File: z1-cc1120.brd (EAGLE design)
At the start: 100 x 50 mm, 11 parts, among them X1 PN61729-S

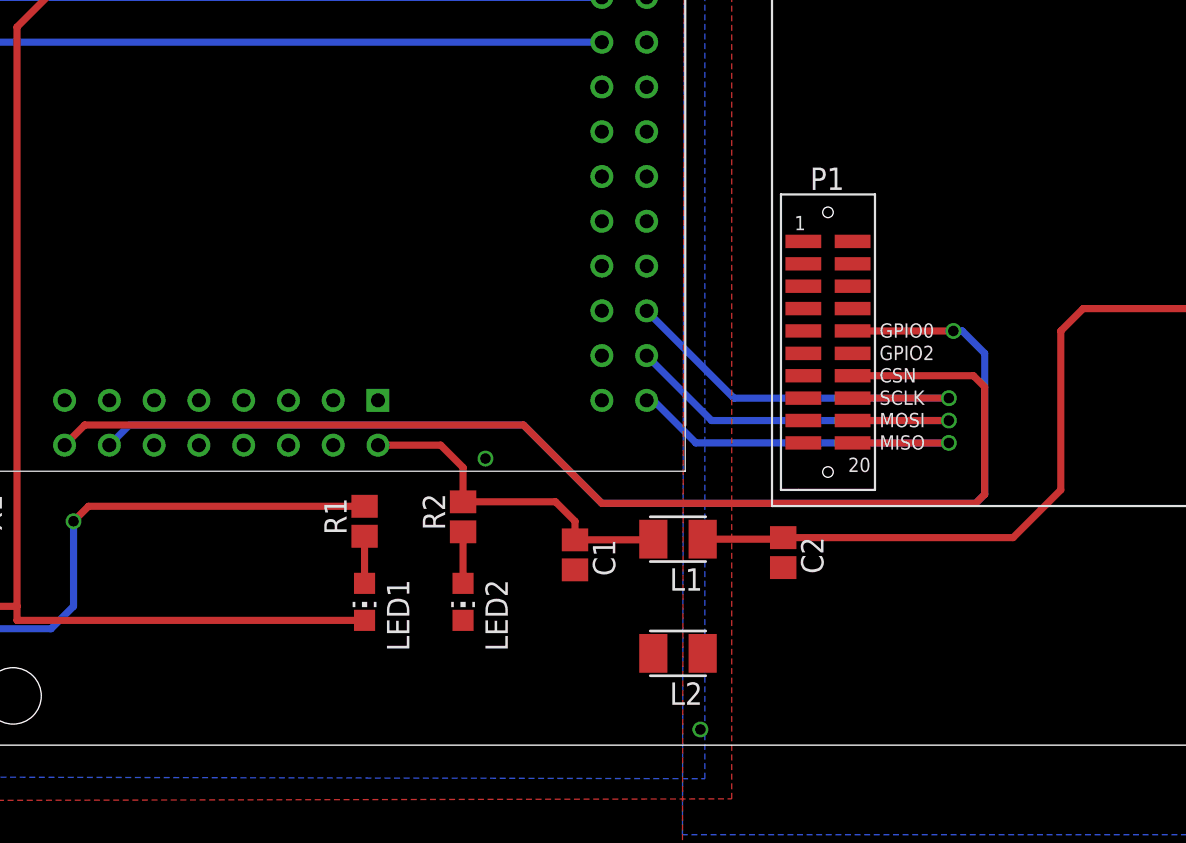
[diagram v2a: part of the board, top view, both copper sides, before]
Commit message: added header to ease radio debug
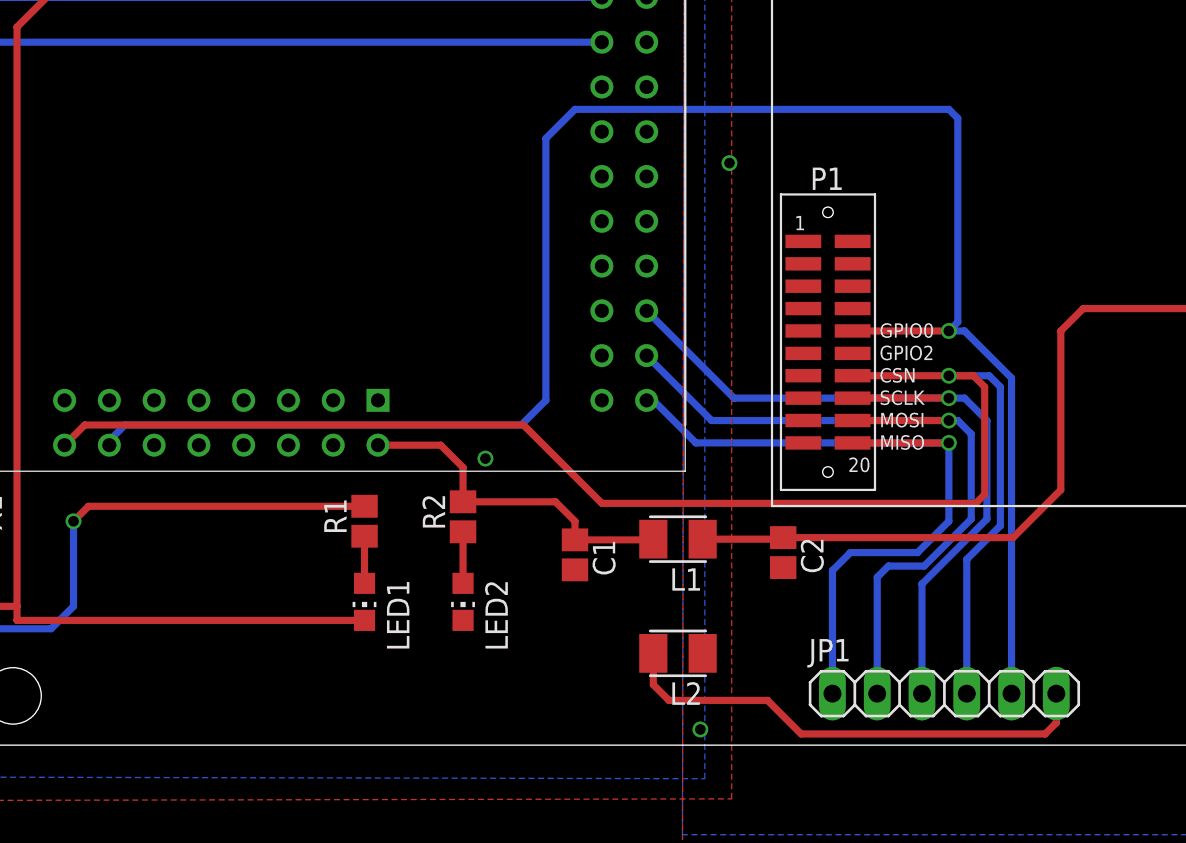
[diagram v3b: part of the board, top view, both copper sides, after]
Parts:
- added JP1: (no value), pinhead:1X06
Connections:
- net GND: now also JP1.6
- net RADIO_CSN: now also JP1.4
- net RADIO_INT: now also JP1.5
- net SPI_CLK: now also JP1.3
- net SPI_SIMO: now also JP1.2
- net SPI_SOMI: now also JP1.1
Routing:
- net RADIO_INT: track 68.2 -> 105.4 mm
- net GND: track 0.00 -> 27.7 mm
- net RADIO_CSN: track 68.6 -> 89.9 mm, vias 0 -> 1
- net SPI_SIMO: track 24.1 -> 43.8 mm
- net SPI_CLK: track 24.7 -> 44.4 mm
- net SPI_SOMI: track 23.6 -> 42.8 mm
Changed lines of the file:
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@@
 <text x="72.898" y="7.747" size="1.778" layer="51">Version 0.1</text>
 <text x="72.898" y="5.715" size="1.778" layer="51">Mountain Sensing</text>
-<text x="72.898" y="3.683" size="1.778" layer="51">PJB</text>
+<text x="22.987" y="1.27" size="1.778" layer="51">PJB</text>
 </plain>
 <attributes>
@@
 <element name="L1" library="resistor" package="L3230M" value="10mH" x="56.388" y="11.684" rot="R180"/>
 <element name="L2" library="resistor" package="L3230M" value="10mH" x="56.388" y="5.207" rot="R180"/>
+<element name="JP1" library="pinhead" package="1X06" value="" x="71.501" y="2.921"/>
 </elements>
 <signals>
@@
 <contactref element="L2" pad="2"/>
 <via x="45.466" y="16.256" extent="1-16" drill="0.6" shape="octagon"/>
+<contactref element="JP1" pad="6"/>
+<wire x1="54.988" y1="5.207" x2="54.988" y2="3.432" width="0.4064" layer="1"/>
+<wire x1="54.988" y1="3.432" x2="55.88" y2="2.54" width="0.4064" layer="1"/>
+<wire x1="55.88" y1="2.54" x2="61.468" y2="2.54" width="0.4064" layer="1"/>
+<wire x1="61.468" y1="2.54" x2="63.373" y2="0.635" width="0.4064" layer="1"/>
+<wire x1="63.373" y1="0.635" x2="77.216" y2="0.635" width="0.4064" layer="1"/>
+<wire x1="77.216" y1="0.635" x2="77.851" y2="1.27" width="0.4064" layer="1"/>
+<wire x1="77.851" y1="1.27" x2="77.851" y2="2.921" width="0.4064" layer="1"/>
 </signal>
 <signal name="VCC_3V3">
@@
 <via x="71.755" y="19.685" extent="1-16" drill="0.6"/>
 <wire x1="71.755" y1="19.685" x2="66.294" y2="19.685" width="0.4064" layer="1"/>
+<contactref element="JP1" pad="3"/>
+<wire x1="71.755" y1="19.685" x2="72.644" y2="19.685" width="0.4064" layer="16"/>
+<wire x1="72.644" y1="19.685" x2="73.914" y2="18.415" width="0.4064" layer="16"/>
+<wire x1="73.914" y1="18.415" x2="73.914" y2="12.827" width="0.4064" layer="16"/>
+<wire x1="73.914" y1="12.827" x2="70.231" y2="9.144" width="0.4064" layer="16"/>
+<wire x1="70.231" y1="9.144" x2="70.231" y2="2.921" width="0.4064" layer="16"/>
 </signal>
 <signal name="SPI_SIMO">
@@
 <via x="71.755" y="18.415" extent="1-16" drill="0.6"/>
 <wire x1="71.755" y1="18.415" x2="66.294" y2="18.415" width="0.4064" layer="1"/>
+<contactref element="JP1" pad="2"/>
+<wire x1="71.755" y1="18.415" x2="72.263" y2="18.415" width="0.4064" layer="16"/>
+<wire x1="72.263" y1="18.415" x2="73.025" y2="17.653" width="0.4064" layer="16"/>
+<wire x1="73.025" y1="17.653" x2="73.025" y2="12.827" width="0.4064" layer="16"/>
+<wire x1="73.025" y1="12.827" x2="70.358" y2="10.16" width="0.4064" layer="16"/>
+<wire x1="70.358" y1="10.16" x2="68.326" y2="10.16" width="0.4064" layer="16"/>
+<wire x1="68.326" y1="10.16" x2="67.691" y2="9.525" width="0.4064" layer="16"/>
+<wire x1="67.691" y1="9.525" x2="67.691" y2="2.921" width="0.4064" layer="16"/>
 </signal>
 <signal name="SPI_SOMI">
@@
 <via x="71.755" y="17.145" extent="1-16" drill="0.6"/>
 <wire x1="71.755" y1="17.145" x2="66.294" y2="17.145" width="0.4064" layer="1"/>
+<contactref element="JP1" pad="1"/>
+<wire x1="71.755" y1="17.145" x2="71.755" y2="12.7" width="0.4064" layer="16"/>
+<wire x1="71.755" y1="12.7" x2="69.977" y2="10.922" width="0.4064" layer="16"/>
+<wire x1="69.977" y1="10.922" x2="66.167" y2="10.922" width="0.4064" layer="16"/>
+<wire x1="66.167" y1="10.922" x2="65.151" y2="9.906" width="0.4064" layer="16"/>
+<wire x1="65.151" y1="9.906" x2="65.151" y2="2.921" width="0.4064" layer="16"/>
 </signal>
 <signal name="RADIO_CSN">
 <contactref element="U$2" pad="CSN"/>
 <contactref element="U$1" pad="C54"/>
-<wire x1="66.294" y1="20.955" x2="73.152" y2="20.955" width="0.4064" layer="1"/>
-<wire x1="73.152" y1="20.955" x2="73.787" y2="20.32" width="0.4064" layer="1"/>
 <wire x1="73.787" y1="20.32" x2="73.787" y2="14.224" width="0.4064" layer="1"/>
 <wire x1="73.787" y1="14.224" x2="73.279" y2="13.716" width="0.4064" layer="1"/>
@@
 <wire x1="47.625" y1="18.161" x2="22.733" y2="18.161" width="0.4064" layer="1"/>
 <wire x1="22.733" y1="18.161" x2="21.59" y2="17.018" width="0.4064" layer="1"/>
+<contactref element="JP1" pad="4"/>
+<wire x1="72.771" y1="2.921" x2="72.771" y2="10.541" width="0.4064" layer="16"/>
+<wire x1="72.771" y1="10.541" x2="74.676" y2="12.446" width="0.4064" layer="16"/>
+<wire x1="74.676" y1="12.446" x2="74.676" y2="20.32" width="0.4064" layer="16"/>
+<wire x1="74.676" y1="20.32" x2="74.041" y2="20.955" width="0.4064" layer="16"/>
+<wire x1="73.787" y1="20.32" x2="73.152" y2="20.955" width="0.4064" layer="1"/>
+<wire x1="73.152" y1="20.955" x2="71.755" y2="20.955" width="0.4064" layer="1"/>
+<via x="71.755" y="20.955" extent="1-16" drill="0.6"/>
+<wire x1="71.755" y1="20.955" x2="74.041" y2="20.955" width="0.4064" layer="16"/>
+<wire x1="66.294" y1="20.955" x2="71.755" y2="20.955" width="0.4064" layer="1"/>
 </signal>
 <signal name="USB_VCC">
@@
 <contactref element="U$1" pad="C52"/>
 <contactref element="U$2" pad="GPIO0"/>
-<wire x1="66.294" y1="23.495" x2="72.009" y2="23.495" width="0.4064" layer="1"/>
-<via x="72.009" y="23.495" extent="1-16" drill="0.6"/>
-<wire x1="72.009" y1="23.495" x2="72.517" y2="23.495" width="0.4064" layer="16"/>
-<wire x1="72.517" y1="23.495" x2="73.787" y2="22.225" width="0.4064" layer="16"/>
-<wire x1="73.787" y1="22.225" x2="73.787" y2="14.224" width="0.4064" layer="16"/>
-<wire x1="73.787" y1="14.224" x2="73.279" y2="13.716" width="0.4064" layer="16"/>
-<wire x1="73.279" y1="13.716" x2="52.07" y2="13.716" width="0.4064" layer="16"/>
-<wire x1="52.07" y1="13.716" x2="47.625" y2="18.161" width="0.4064" layer="16"/>
-<wire x1="47.625" y1="18.161" x2="25.273" y2="18.161" width="0.4064" layer="16"/>
-<wire x1="25.273" y1="18.161" x2="24.13" y2="17.018" width="0.4064" layer="16"/>
+<contactref element="JP1" pad="5"/>
+<wire x1="24.13" y1="17.018" x2="24.13" y2="17.272" width="0.4064" layer="16"/>
+<wire x1="24.13" y1="17.272" x2="25.019" y2="18.161" width="0.4064" layer="16"/>
+<wire x1="25.019" y1="18.161" x2="47.498" y2="18.161" width="0.4064" layer="16"/>
+<wire x1="47.498" y1="18.161" x2="48.895" y2="19.558" width="0.4064" layer="16"/>
+<wire x1="48.895" y1="19.558" x2="48.895" y2="34.417" width="0.4064" layer="16"/>
+<wire x1="48.895" y1="34.417" x2="50.546" y2="36.068" width="0.4064" layer="16"/>
+<wire x1="50.546" y1="36.068" x2="71.755" y2="36.068" width="0.4064" layer="16"/>
+<wire x1="71.755" y1="36.068" x2="72.263" y2="35.56" width="0.4064" layer="16"/>
+<wire x1="72.263" y1="35.56" x2="72.263" y2="24.003" width="0.4064" layer="16"/>
+<wire x1="72.263" y1="24.003" x2="71.755" y2="23.495" width="0.4064" layer="16"/>
+<via x="71.755" y="23.495" extent="1-16" drill="0.6"/>
+<wire x1="71.755" y1="23.495" x2="66.294" y2="23.495" width="0.4064" layer="1"/>
+<wire x1="71.755" y1="23.495" x2="72.644" y2="23.495" width="0.4064" layer="16"/>
+<wire x1="72.644" y1="23.495" x2="75.311" y2="20.828" width="0.4064" layer="16"/>
+<wire x1="75.311" y1="20.828" x2="75.311" y2="2.921" width="0.4064" layer="16"/>
 </signal>
 <signal name="N$24">
@@
 <via x="94.107" y="3.175" extent="1-16" drill="0.6" shape="octagon"/>
 <via x="96.901" y="5.715" extent="1-16" drill="0.6" shape="octagon"/>
+<via x="59.309" y="33.02" extent="1-16" drill="0.6"/>
 </signal>
 <signal name="RADIO_3V3">
